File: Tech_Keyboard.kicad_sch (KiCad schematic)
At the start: 36 parts, among them SW2 RotaryEncoder, U1 MCU_Seeed_XIAO_RP2040

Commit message: wiring done
wired up pcb and fixed schematic... kind mad cuz i spent 3 hours and forgot to hit record...
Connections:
- net Column 0: no longer D1.1 (K), D1.2 (A), D10.1 (K), D10.2 (A), D11.1 (K), D11.2 (A), D12.1 (K), D12.2 (A), D13.1 (K), D13.2 (A), D14.1 (K), D14.2 (A), D15.1 (K), D15.2 (A), D16.1 (K), D16.2 (A), D17.1 (K), D17.2 (A), D2.1 (K), D2.2 (A), D3.1 (K), D3.2 (A), D4.1 (K), D4.2 (A), D5.1 (K), D5.2 (A), D6.1 (K), D6.2 (A), D7.1 (K), D7.2 (A), D8.1 (K), D8.2 (A), D9.1 (K), D9.2 (A), S1.2, S10.1, S10.2, S11.1, S11.2, S12.2, S13.1, S13.2, S14.1, S14.2, S15.1, S15.2, S16.2, S17.1, S17.2, S2.1, S2.2, S3.1, S3.2, S4.1, S4.2, S5.2, S6.1, S6.2, S7.1, S7.2, S8.1, S8.2, S9.2, U1.1 (PA02_A0_D0), U1.10 (PA5_A9_D9_MISO), U1.11 (PA6_A10_D10_MOSI), U1.2 (PA4_A1_D1), U1.3 (PA10_A2_D2), U1.5 (PA8_A4_D4_SDA), U1.6 (PA9_A5_D5_SCL), U1.7 (PB08_A6_D6_TX)
- new net Column 1: S10.1, S13.1, S2.1, S6.1, U1.3 (PA10_A2_D2)
- new net Column 2: S11.1, S14.1, S17.1, S3.1, S7.1, U1.2 (PA4_A1_D1)
- new net Column 3: S15.1, S4.1, S8.1, U1.1 (PA02_A0_D0)
- new net Row 0: D1.1 (K), D1.2 (A), D2.1 (K), D2.2 (A), D3.1 (K), D3.2 (A), D4.1 (K), D4.2 (A), S1.2, S2.2, S3.2, S4.2, U1.5 (PA8_A4_D4_SDA)
- new net Row 1: D5.1 (K), D5.2 (A), D6.1 (K), D6.2 (A), D7.1 (K), D7.2 (A), D8.1 (K), D8.2 (A), S5.2, S6.2, S7.2, S8.2, U1.6 (PA9_A5_D5_SCL)
- new net Row 2: D10.1 (K), D10.2 (A), D11.1 (K), D11.2 (A), D9.1 (K), D9.2 (A), S10.2, S11.2, S9.2, U1.7 (PB08_A6_D6_TX)
- new net Row 3: D12.1 (K), D12.2 (A), D13.1 (K), D13.2 (A), D14.1 (K), D14.2 (A), D15.1 (K), D15.2 (A), S12.2, S13.2, S14.2, S15.2, U1.10 (PA5_A9_D9_MISO)
- new net Row 4: D16.1 (K), D16.2 (A), D17.1 (K), D17.2 (A), S16.2, S17.2, U1.11 (PA6_A10_D10_MOSI)

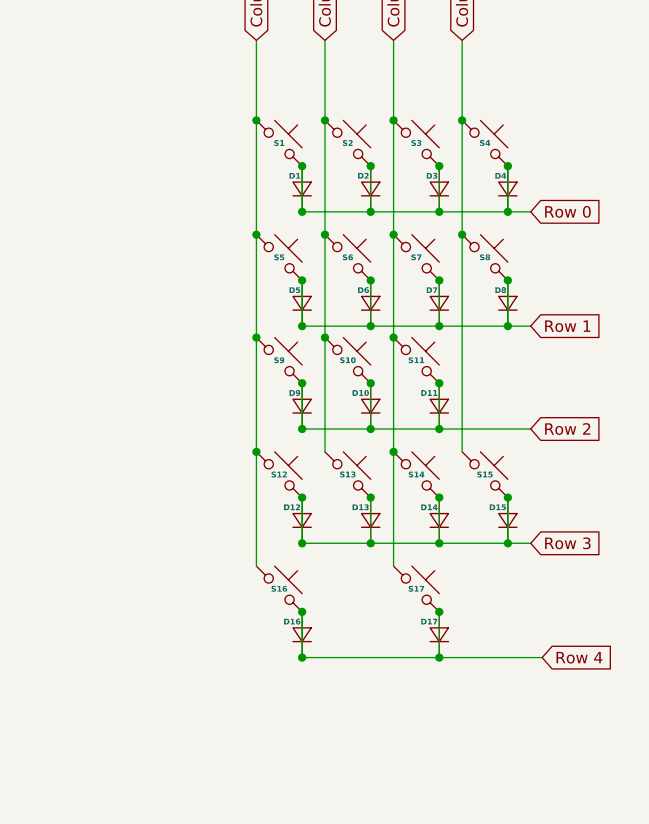
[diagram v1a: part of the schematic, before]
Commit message: 3D model being worked on, PCB finished
https://a360.co/41LIHIl
fusion 360 file
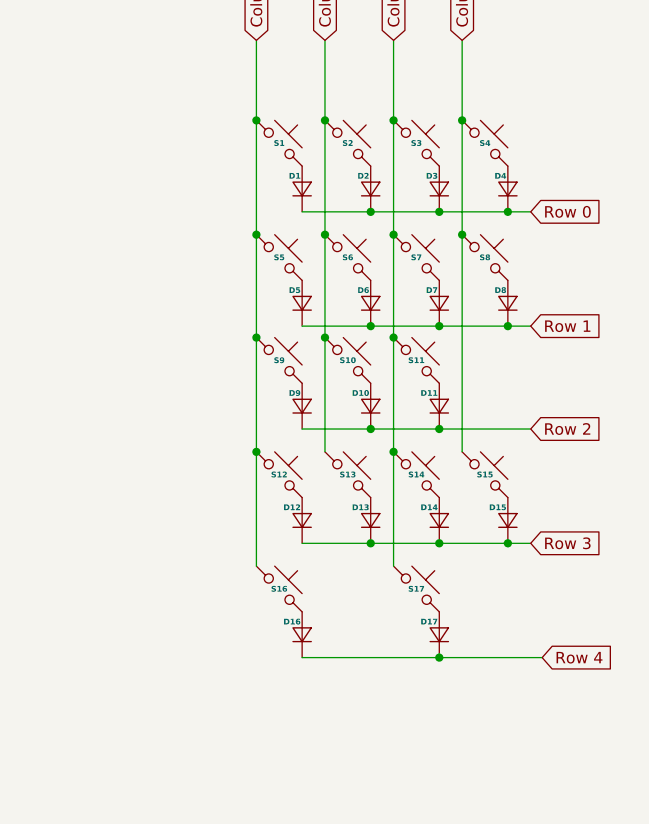
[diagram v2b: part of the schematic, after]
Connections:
- net Row 0: no longer D1.2 (A), D2.2 (A), D3.2 (A), D4.2 (A), S1.2, S2.2, S3.2, S4.2
- net Row 1: no longer D5.2 (A), D6.2 (A), D7.2 (A), D8.2 (A), S5.2, S6.2, S7.2, S8.2
- net Row 2: no longer D10.2 (A), D11.2 (A), D9.2 (A), S10.2, S11.2, S9.2
- net Row 3: no longer D12.2 (A), D13.2 (A), D14.2 (A), D15.2 (A), S12.2, S13.2, S14.2, S15.2
- net Row 4: no longer D16.2 (A), D17.2 (A), S16.2, S17.2
- new net: D1.2 (A), S1.2
- new net: D8.2 (A), S8.2
- new net: D17.2 (A), S17.2
- new net: D11.2 (A), S11.2
- new net: D10.2 (A), S10.2
- new net: D12.2 (A), S12.2
- new net: D3.2 (A), S3.2
- new net: D15.2 (A), S15.2
- new net: D5.2 (A), S5.2
- new net: D6.2 (A), S6.2
- new net: D14.2 (A), S14.2
- new net: D7.2 (A), S7.2
- new net: D2.2 (A), S2.2
- new net: D4.2 (A), S4.2
- new net: D16.2 (A), S16.2
- new net: D13.2 (A), S13.2
- new net: D9.2 (A), S9.2
